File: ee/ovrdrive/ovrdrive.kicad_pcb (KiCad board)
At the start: 4 copper layers, 36.4 x 15 mm, 47 parts, among them J2 USB3_A, J4 Micro_SD_Card_Det_Hirose_DM3AT, SW1 SW_Push, U1 CH569W, U2 TLV62569DBV, U3 TLV62569DBV, Y2 30Mhz

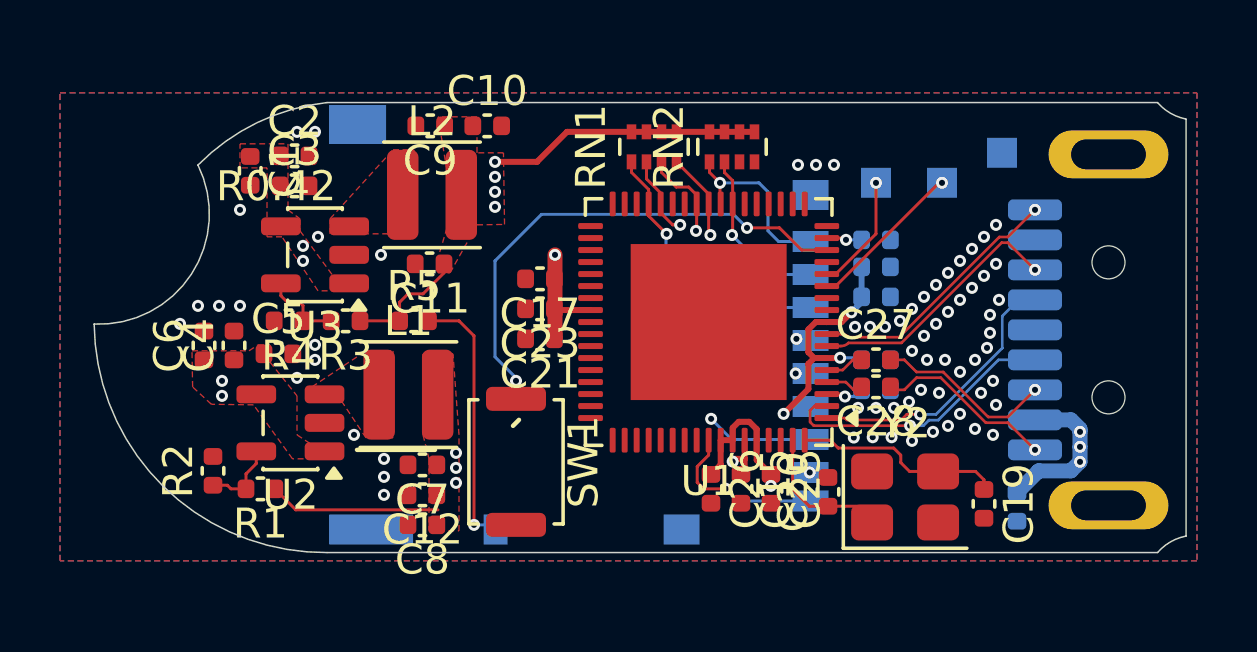
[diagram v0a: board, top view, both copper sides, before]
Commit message: Finished routing of PCB.
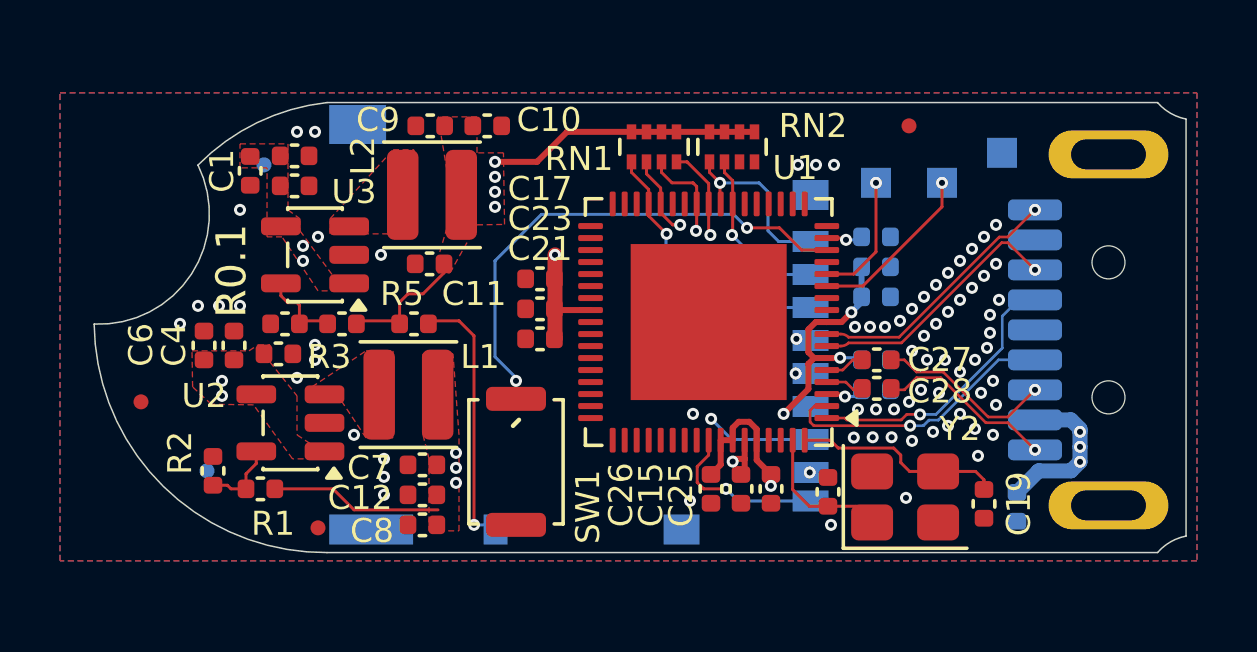
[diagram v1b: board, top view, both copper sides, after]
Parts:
- added FID1: Fiducial, Fiducial:Fiducial_0.5mm_Mask1mm, B.Cu at (113.7, 98.7)
- added FID2: Fiducial, Fiducial:Fiducial_0.5mm_Mask1mm, F.Cu at (115.5, 110.8)
- added FID3: Fiducial, Fiducial:Fiducial_0.5mm_Mask1mm, F.Cu at (135.2, 97.4)
- added FID4: Fiducial, Fiducial:Fiducial_0.5mm_Mask1mm, F.Cu at (109.6, 106.6)
- added FID5: Fiducial, Fiducial:Fiducial_0.5mm_Mask1mm, B.Cu at (111.8, 108.9)
- added FID6: Fiducial, Fiducial:Fiducial_0.5mm_Mask1mm, B.Cu at (136.4, 110.5)
- moved R3 0.16 mm to (116.3, 104.0)
- moved R4 0.16 mm to (114.4, 104.0)
- moved C18 0.10 mm to (134.1, 101.1)
- moved R5 0.10 mm to (118.7, 104.0)
- moved C28 0.06 mm to (134.1, 106.2)
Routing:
- net VBUS: track 46.2 -> 45.7 mm
- net GND: vias 65 -> 70
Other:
- board text added: "R0.1"
- board text removed: "OVRDRIVE V2 Interrupt Labs"
- board text removed: "R0.42"
